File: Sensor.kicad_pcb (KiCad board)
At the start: 2 copper layers, 49.5 x 49.5 mm, 51 parts, among them IC1 STM32L051K8T6, P1 CONN_02X04, P2 CONN_02X04, P3 CONN_01X02, Q1 AO3401, SW1 SW_PUSH, U1 MCP60x4, U2 HTU21D, U3 PIR, U4 TPS79718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

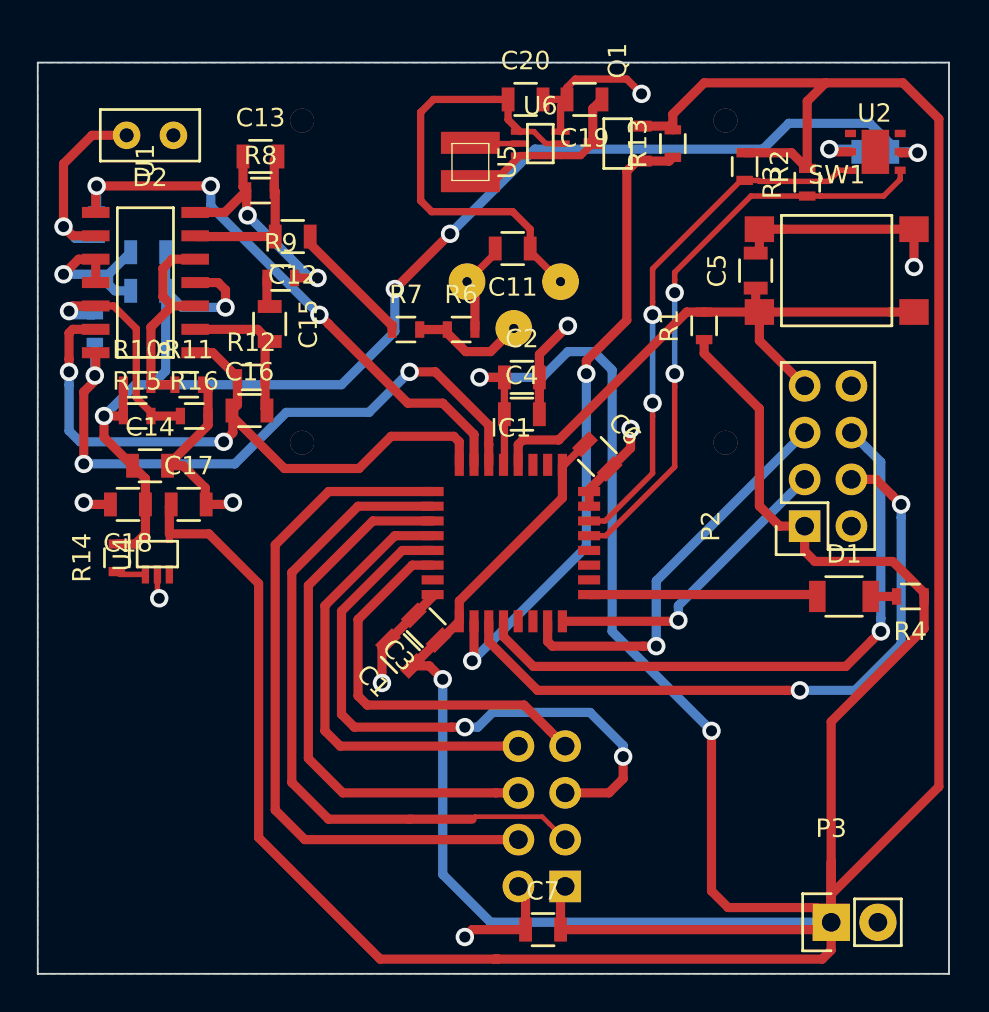
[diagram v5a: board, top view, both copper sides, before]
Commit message: Add extra switch for user defined functionality
 * reroute pcb

Signed-off-by: pluyckx <philip.luyckx@gmail.com>
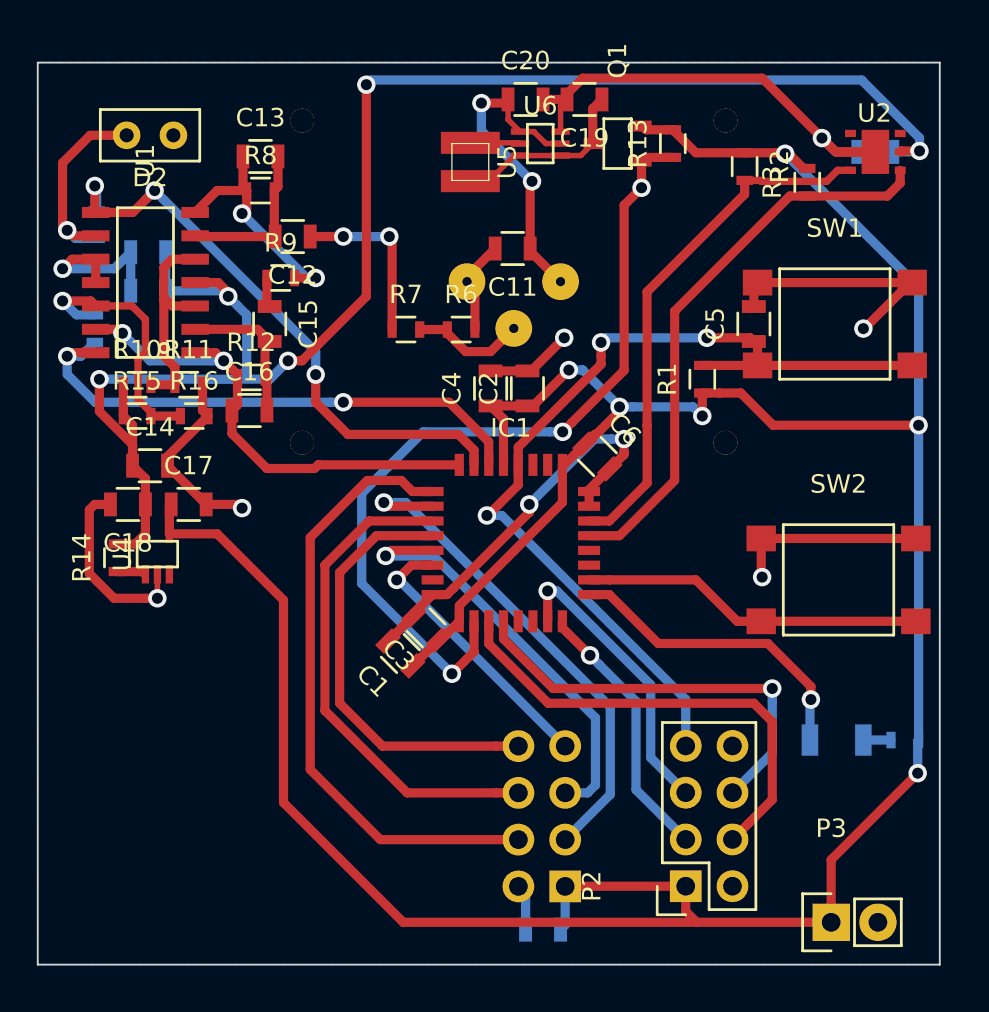
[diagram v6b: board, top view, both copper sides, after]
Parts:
- added SW2: SW_PUSH, CustomSmd:MicroSwitch_6x6mm, F.Cu at (161.9, 97.4)
- C7, D1, R4: moved to B.Cu
- moved P2 20.6 mm to (153.6, 114.0)
- moved D1 7.81 mm to (161.8, 106.1)
- moved R4 7.81 mm to (165.5, 106.1)
- moved SW1 2.90 mm to (161.7, 83.5)
- moved C5 2.90 mm to (157.3, 83.5)
- moved R1 2.90 mm to (154.5, 86.5)
- moved C4 2.20 mm to (143.0, 87.0), turned to 90 degrees
- moved C2 0.67 mm to (145.0, 87.0), turned to 90 degrees
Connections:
- IC1 pad 26: Net-(IC1-Pad26) -> BTN_User
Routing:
- net +BATT: track 296.0 -> 170.1 mm, vias 3 -> 6
- net GND: track 73.3 -> 116.5 mm, vias 11 -> 9
- net MCU_RST: track 32.0 -> 50.7 mm, vias 0 -> 3
- net BTN_User: track 0.00 -> 18.7 mm
- net +1V8: track 79.7 -> 91.4 mm
- net ADC_Motion: track 38.1 -> 27.0 mm
- net UART_RX: track 34.3 -> 23.2 mm
- net UART_TX: track 36.5 -> 25.7 mm, vias 2 -> 0
- net SPI_RF_MOSI: track 33.9 -> 23.2 mm, vias 2 -> 1
- net Enable5V: track 35.1 -> 45.7 mm, vias 2 -> 3
- net RF_CSN: track 37.0 -> 27.9 mm, vias 0 -> 1
- net MotionSensor_V+: track 24.5 -> 17.6 mm, vias 0 -> 2
- net RF_IRQ: track 21.8 -> 15.2 mm, vias 0 -> 1
- net SWDIO: track 22.0 -> 16.0 mm
- net DIG_Motion: track 35.6 -> 30.1 mm, vias 3 -> 2
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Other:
- board size 49.5 x 49.5 mm -> 49 x 49 mm

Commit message: Remove unnecessary via
Signed-off-by: pluyckx <philip.luyckx@gmail.com>
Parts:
- moved R3 8.12 mm to (153.8, 80.8), turned to 0 degrees
- moved R2 4.93 mm to (153.8, 78.9), turned to 180 degrees
- moved C9 0.05 mm to (163.8, 74.2), turned to 0 degrees
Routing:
- net +BATT: track 170.1 -> 175.7 mm
- net GND: track 116.5 -> 121.5 mm, vias 9 -> 10
- net HTU21_SDA: track 28.7 -> 33.3 mm, vias 0 -> 2
- net +1V8: track 91.4 -> 89.4 mm
- net HTU21_SCK: track 30.9 -> 32.2 mm
- net Net-(U2-Pad4): track 0.00 -> 0.70 mm
- net Net-(U2-Pad3): track 0.00 -> 0.60 mm
- net Enable5V: vias 3 -> 2

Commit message: Update QFN package for easier soldering
Signed-off-by: pluyckx <philip.luyckx@gmail.com>
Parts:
- moved U2 1.56 mm to (163.7, 74.2)
- moved C9 1.55 mm to (163.8, 75.7)
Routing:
- net GND: track 121.5 -> 126.6 mm, vias 10 -> 11
- net HTU21_SDA: track 33.3 -> 35.1 mm
- net +BATT: track 175.7 -> 174.1 mm
- net +1V8: track 89.4 -> 88.0 mm
- net HTU21_SCK: track 32.2 -> 31.6 mm
